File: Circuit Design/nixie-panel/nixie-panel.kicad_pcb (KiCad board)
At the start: 2 copper layers, 119.4 x 109.5 mm, 644 parts, among them J1 Conn_01x06, J2 Conn_01x06, U4 IS31FL3731, U5 IS31FL3731, U6 IS31FL3731, U7 IS31FL3731

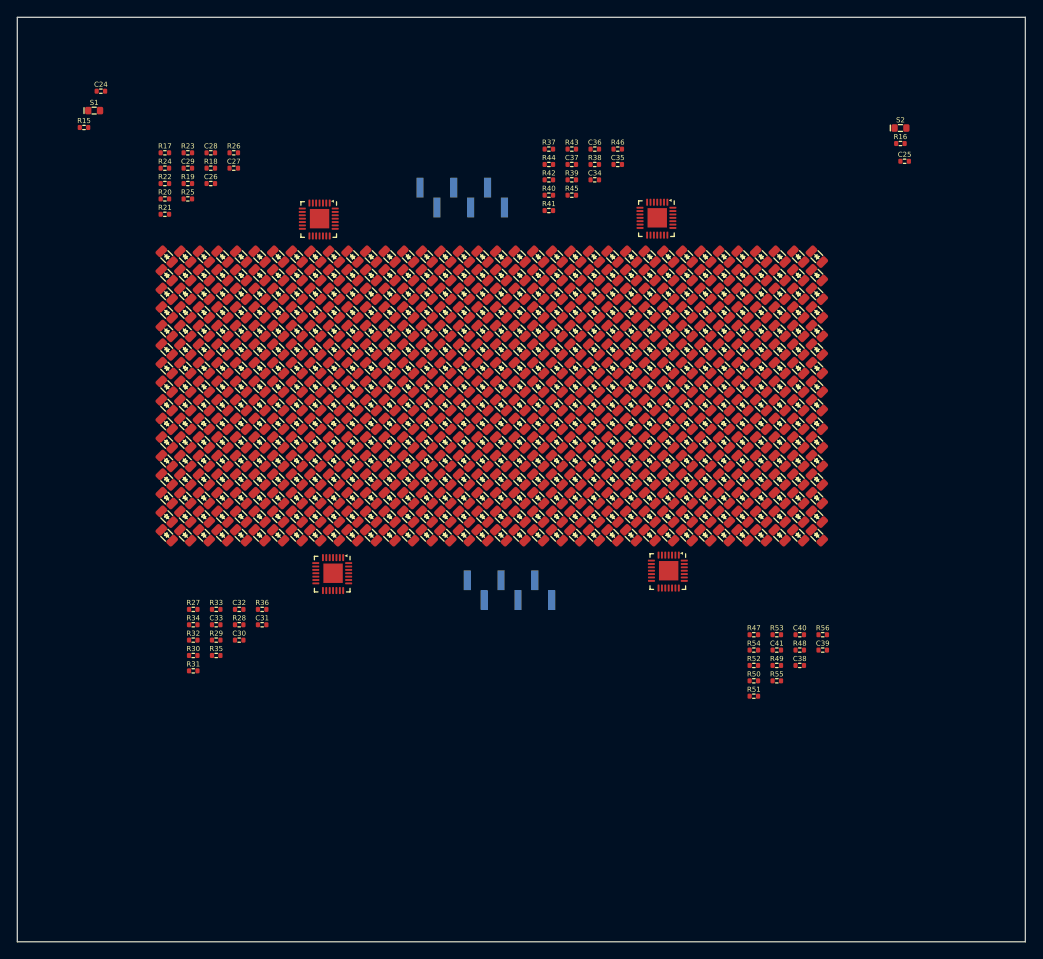
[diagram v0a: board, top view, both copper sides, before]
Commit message: routing is done (mostly). Paused routing, waiting for spaceClaim
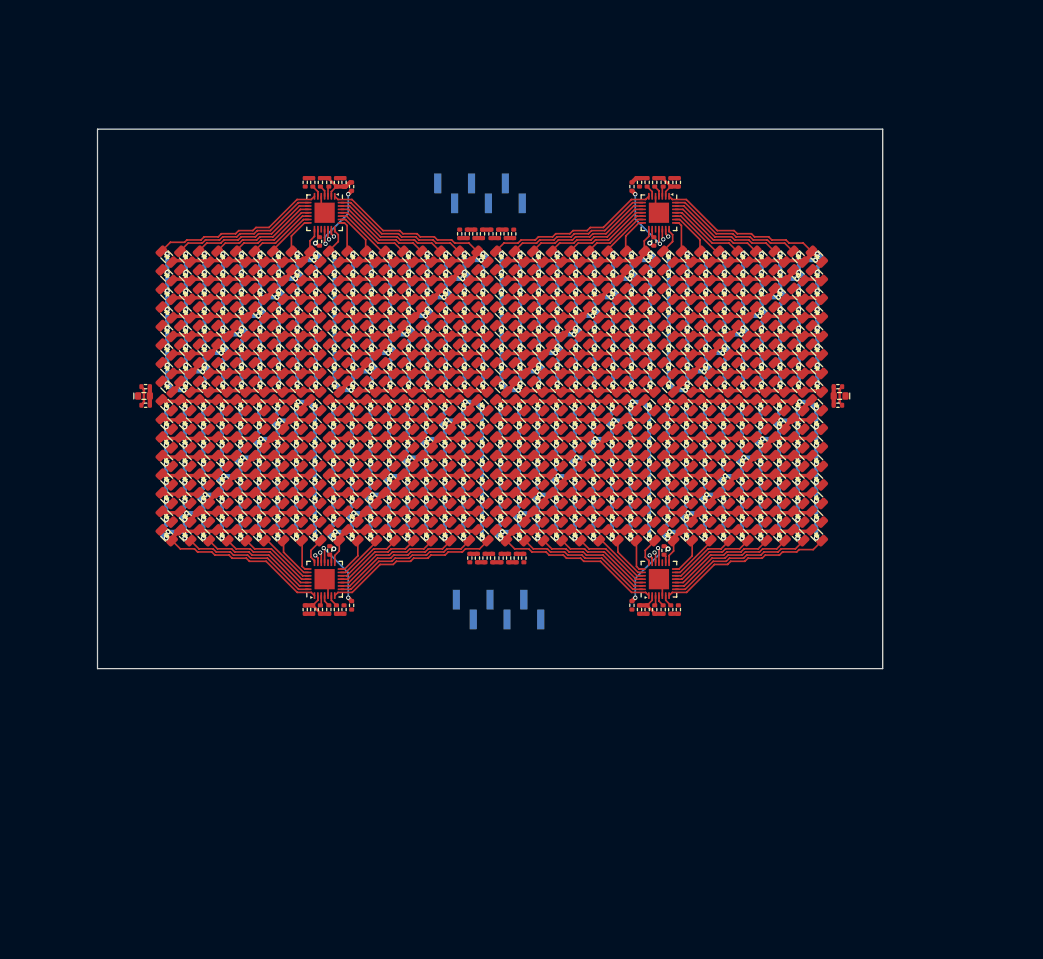
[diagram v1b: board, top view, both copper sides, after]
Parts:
- removed R23, R24, R33, R34, R43, R44, R53, R54: 1R, CoF_Resistor:R-0402
- moved R21 37.7 mm to (120.4, 49.3), turned to -90 degrees
- moved R20 37.0 mm to (119.5, 49.3), turned to -90 degrees
- moved R32 36.8 mm to (121.6, 87.7), turned to 90 degrees
- moved R30 35.6 mm to (119.8, 87.7), turned to 90 degrees
- moved R22 35.4 mm to (117.7, 49.3), turned to -90 degrees
- moved C24 35.4 mm to (80.5, 67.4), turned to 180 degrees
- moved R31 35.4 mm to (118.9, 87.7), turned to 90 degrees
- moved S1 34.3 mm to (80.3, 68.5)
- moved R49 34.2 mm to (123.5, 87.7), turned to 90 degrees
- moved R15 33.7 mm to (80.5, 69.6), turned to 180 degrees
- moved R19 33.6 mm to (118.6, 49.3), turned to -90 degrees
- moved R29 33.3 mm to (120.7, 87.7), turned to 90 degrees
- moved S2 32.5 mm to (162.7, 68.5), turned to 180 degrees
- moved R52 32.5 mm to (122.6, 87.7), turned to 90 degrees
- moved R16 31.9 mm to (162.5, 69.6)
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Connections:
- R17 pad 2: Net-(R17-Pad2) -> /region1/LED Driver/SDB
- R18 pad 2: Net-(R18-Pad2) -> /region1/LED Driver/INTB
- R27 pad 2: Net-(R27-Pad2) -> /region2/LED Driver/SDB
- R28 pad 2: Net-(R28-Pad2) -> /region2/LED Driver/INTB
- R37 pad 2: Net-(R37-Pad2) -> /region3/LED Driver/SDB
- R38 pad 2: Net-(R38-Pad2) -> /region3/LED Driver/INTB
- R47 pad 2: Net-(R47-Pad2) -> /region4/LED Driver/SDB
- R48 pad 2: Net-(R48-Pad2) -> /region4/LED Driver/INTB
- U4 pad 3: Net-(R17-Pad2) -> /region1/LED Driver/SDB
- U4 pad 4: Net-(R18-Pad2) -> /region1/LED Driver/INTB
- U5 pad 3: Net-(R27-Pad2) -> /region2/LED Driver/SDB
- U5 pad 4: Net-(R28-Pad2) -> /region2/LED Driver/INTB
- U6 pad 3: Net-(R37-Pad2) -> /region3/LED Driver/SDB
- U6 pad 4: Net-(R38-Pad2) -> /region3/LED Driver/INTB
- U7 pad 3: Net-(R47-Pad2) -> /region4/LED Driver/SDB
- U7 pad 4: Net-(R48-Pad2) -> /region4/LED Driver/INTB
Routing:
- net /region1/LED Driver/CB1: track 0.00 -> 62.4 mm, vias 0 -> 9
- net /region2/LED Driver/CB1: track 0.00 -> 62.4 mm, vias 0 -> 9
- net /region3/LED Driver/CB1: track 0.00 -> 62.4 mm, vias 0 -> 9
- net /region4/LED Driver/CB1: track 0.00 -> 62.4 mm, vias 0 -> 9
- net /region4/LED Driver/CA9: track 0.00 -> 60.4 mm, vias 0 -> 8
- net /region2/LED Driver/CA9: track 0.00 -> 60.4 mm, vias 0 -> 8
- net /region1/LED Driver/CA9: track 0.00 -> 60.4 mm, vias 0 -> 8
- net /region3/LED Driver/CA9: track 0.00 -> 60.4 mm, vias 0 -> 8
- net /region1/LED Driver/CB2: track 0.00 -> 58.5 mm, vias 0 -> 9
- net /region4/LED Driver/CB2: track 0.00 -> 58.5 mm, vias 0 -> 9
- net /region3/LED Driver/CB2: track 0.00 -> 58.5 mm, vias 0 -> 9
- net /region2/LED Driver/CB2: track 0.00 -> 58.5 mm, vias 0 -> 9
- net /region3/LED Driver/CA8: track 0.00 -> 57.7 mm, vias 0 -> 9
- net /region1/LED Driver/CA8: track 0.00 -> 57.7 mm, vias 0 -> 9
- net /region4/LED Driver/CA8: track 0.00 -> 57.7 mm, vias 0 -> 9
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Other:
- board size 119.4 x 109.5 mm -> 93 x 63.9 mm
